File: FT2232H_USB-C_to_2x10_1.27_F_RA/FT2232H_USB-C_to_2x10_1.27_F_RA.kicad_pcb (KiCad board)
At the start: 4 copper layers, 39.8 x 60 mm, 42 parts, among them J1 USB_B_Micro, J2 Conn_02x10_Odd_Even, J3 Conn_02x10_Odd_Even, U1 FT2232HL, U2 93C46BT-I_OT, U3 USBLC6-2SC6, U4 MIC5504-3.3YM5, X1 DSC60xx

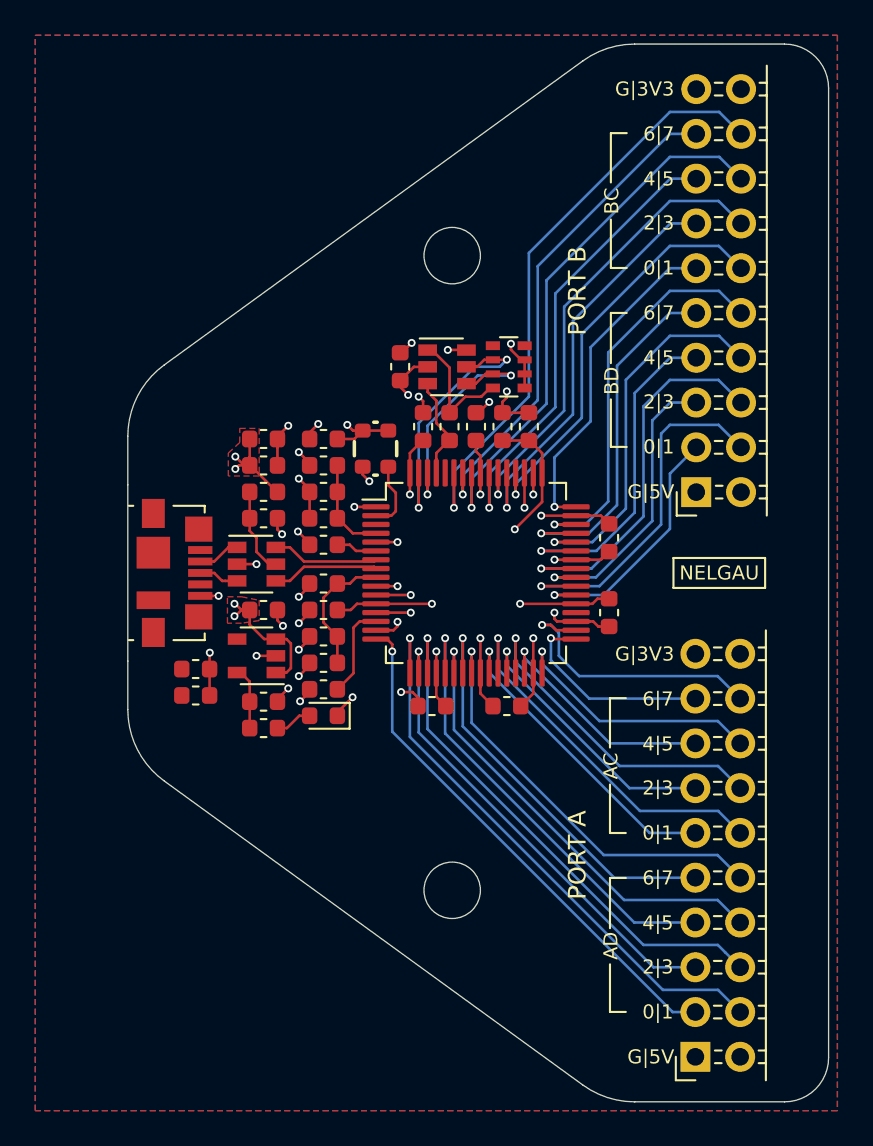
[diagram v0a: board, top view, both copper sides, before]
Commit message: Use USB-C connector instead of micro-USB
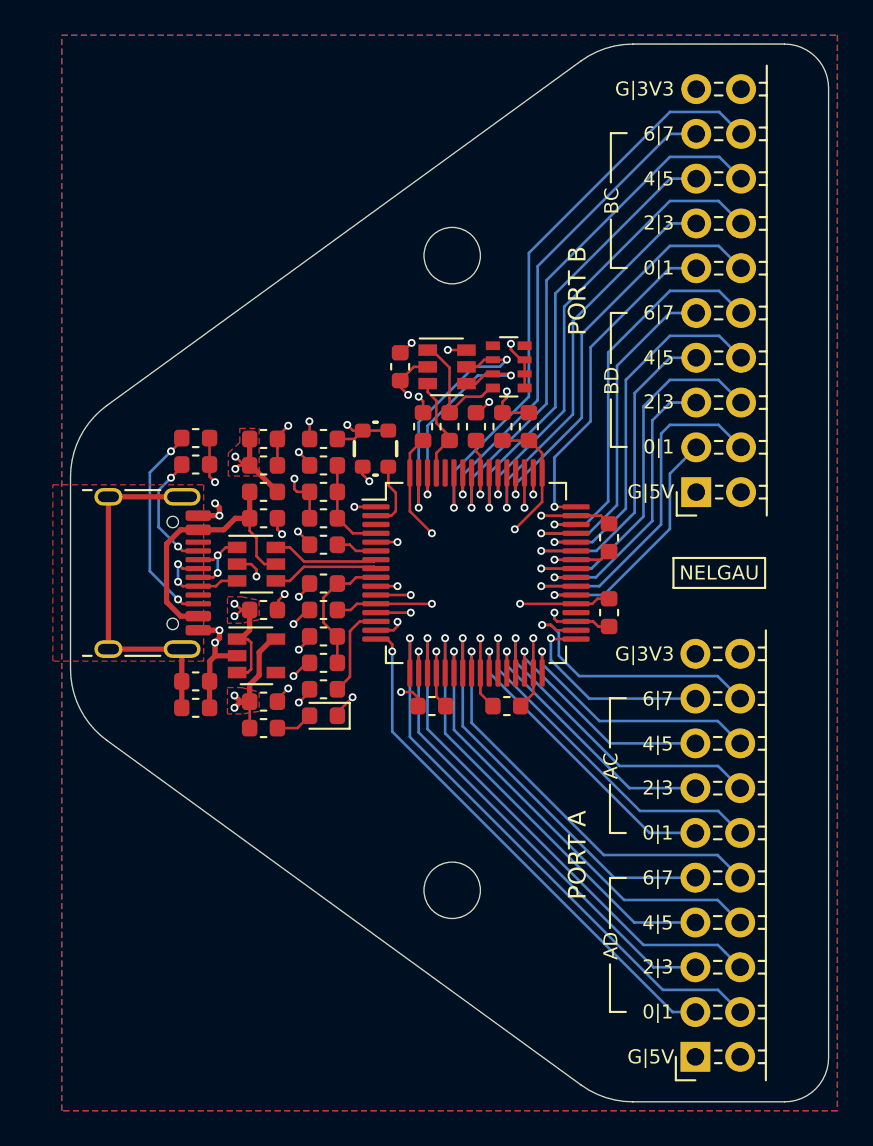
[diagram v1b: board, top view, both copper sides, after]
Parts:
- added R7: 5k1, Resistor_SMD:R_0603_1608Metric, F.Cu at (145.1, 89.4)
- added R8: 5k1, Resistor_SMD:R_0603_1608Metric, F.Cu at (145.1, 90.9)
- J1: value USB_B_Micro -> USB_C_USB2.0; footprint Connector_USB:USB_Micro-B_Molex_47346-0001 -> ng_conn:USB_C_Receptacle_HRO_TYPE-C-31-M-12
- moved J1 2.70 mm to (141.2, 97.0)
- moved R1 2.20 mm to (145.1, 104.7), turned to 0 degrees
- moved C6 0.80 mm to (145.1, 103.2)
- turned U4 to 0 degrees
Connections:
- R1 pad 1: GND -> /USB_SHD
- R1 pad 2: /USB_SHD -> GND
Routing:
- net /USB_SHD: track 0.00 -> 20.5 mm
- net /USB_CC2: track 0.00 -> 11.8 mm, vias 0 -> 2
- net /USB_VBUS: track 4.95 -> 15.8 mm
- net GND: track 53.8 -> 62.2 mm, vias 31 -> 33
- net /USB_CC1: track 0.00 -> 6.90 mm, vias 0 -> 2
- net P3V3: track 30.8 -> 34.9 mm, vias 12 -> 14
- net /xUSB_D+: track 2.28 -> 5.83 mm, vias 0 -> 2
- net P1V8: track 21.6 -> 24.3 mm
- net /xUSB_D-: track 2.42 -> 4.70 mm, vias 0 -> 2
- added copper zone on F.Cu, net /USB_SHD
- added copper zone on F.Cu, net P3V3
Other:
- board size 39.8 x 60 mm -> 43 x 60 mm

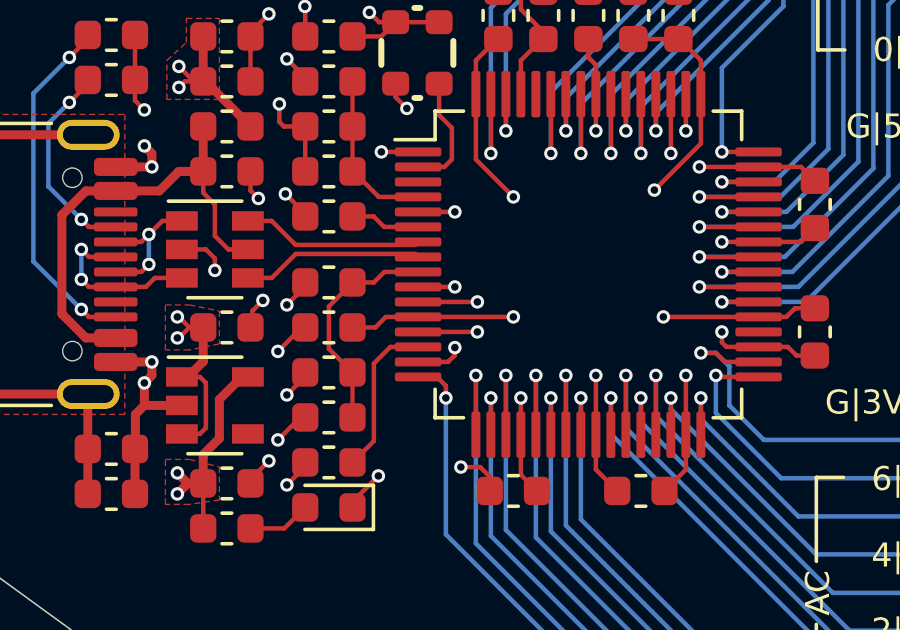
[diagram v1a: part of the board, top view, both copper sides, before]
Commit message: Reduce via usage on FT2232 ground connections
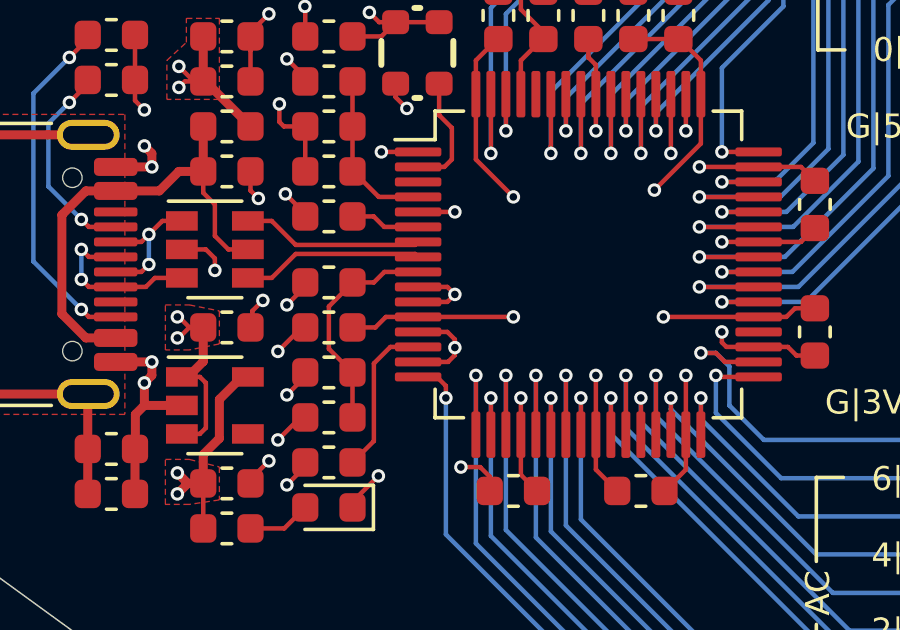
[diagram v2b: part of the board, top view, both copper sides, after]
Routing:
- net GND: track 62.2 -> 61.3 mm, vias 33 -> 31
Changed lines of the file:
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@@
     (thickness 1.2)
     (drawings 63)
-    (tracks 612)
+    (tracks 614)
     (zones 0)
     (modules 44)
@@
   (layers
     (0 F.Cu signal)
-    (1 "In1(GND).Cu" power)
-    (2 "In2(PWR).Cu" power)
+    (1 "In1(GND).Cu" power hide)
+    (2 "In2(PWR).Cu" power hide)
     (31 B.Cu signal)
     (32 B.Adhes user hide)
@@
   )
   (setup
-    (last_trace_width 0.3)
+    (last_trace_width 0.15)
     (user_trace_width 0.3)
     (user_trace_width 0.6)
@@
   (via (at 161.25 100.728) (size 0.45) (drill 0.25) (layers F.Cu B.Cu) (net 1))
   (segment (start 161.25 102.703) (end 161.25 100.728) (width 0.15) (layer F.Cu) (net 1))
-  (via (at 157.3 98.278) (size 0.45) (drill 0.25) (layers F.Cu B.Cu) (net 1))
-  (segment (start 155.325 98.278) (end 157.3 98.278) (width 0.15) (layer F.Cu) (net 1))
-  (via (at 156.54999 97.778) (size 0.45) (drill 0.25) (layers F.Cu B.Cu) (net 1))
-  (segment (start 155.325 97.778) (end 156.54999 97.778) (width 0.15) (layer F.Cu) (net 1))
   (segment (start 167.45 93.778) (end 166.675 93.778) (width 0.15) (layer F.Cu) (net 1))
   (segment (start 168.0875 93.778) (end 167.45 93.778) (width 0.15) (layer F.Cu) (net 1))
@@
   (segment (start 162.75 87.078) (end 162.75 86.728) (width 0.15) (layer F.Cu) (net 1))
   (segment (start 162.5 87.328) (end 162.75 87.078) (width 0.15) (layer F.Cu) (net 1))
-  (segment (start 155.325 99.278) (end 157.3 99.278) (width 0.15) (layer F.Cu) (net 1))
-  (via (at 157.3 99.278) (size 0.45) (drill 0.25) (layers F.Cu B.Cu) (net 1))
   (via (at 156.55 99.799992) (size 0.45) (drill 0.25) (layers F.Cu B.Cu) (net 1))
-  (segment (start 156.55 100.05) (end 156.55 99.799992) (width 0.15) (layer F.Cu) (net 1))
-  (segment (start 156.322 100.278) (end 156.55 100.05) (width 0.15) (layer F.Cu) (net 1))
-  (segment (start 155.325 100.278) (end 156.322 100.278) (width 0.15) (layer F.Cu) (net 1))
   (via (at 150.00001 94.828) (size 0.45) (drill 0.25) (layers F.Cu B.Cu) (net 1))
   (segment (start 149.7375 94.56549) (end 150.00001 94.828) (width 0.15) (layer F.Cu) (net 1))
@@
   (segment (start 148.25 96.528) (end 148.549996 96.827996) (width 0.15) (layer F.Cu) (net 1))
   (segment (start 147.45 96.528) (end 148.25 96.528) (width 0.15) (layer F.Cu) (net 1))
+  (segment (start 156.55 100.05) (end 156.55 99.799992) (width 0.15) (layer F.Cu) (net 1))
+  (segment (start 156.322 100.278) (end 156.55 100.05) (width 0.15) (layer F.Cu) (net 1))
+  (segment (start 155.325 100.278) (end 156.322 100.278) (width 0.15) (layer F.Cu) (net 1))
+  (segment (start 156.55 99.528) (end 156.55 99.799992) (width 0.15) (layer F.Cu) (net 1))
+  (segment (start 156.3 99.278) (end 156.55 99.528) (width 0.15) (layer F.Cu) (net 1))
+  (segment (start 155.325 99.278) (end 156.3 99.278) (width 0.15) (layer F.Cu) (net 1))
+  (segment (start 156.3 97.778) (end 156.55 98.028) (width 0.15) (layer F.Cu) (net 1))
+  (segment (start 156.3 98.278) (end 156.55 98.028) (width 0.15) (layer F.Cu) (net 1))
+  (via (at 156.55 98.028) (size 0.45) (drill 0.25) (layers F.Cu B.Cu) (net 1))
+  (segment (start 155.325 97.778) (end 156.3 97.778) (width 0.15) (layer F.Cu) (net 1))
+  (segment (start 155.325 98.278) (end 156.3 98.278) (width 0.15) (layer F.Cu) (net 1))
   (segment (start 162.975 89.5155) (end 164 89.5155) (width 0.15) (layer F.Cu) (net 2))
   (segment (start 162.5 89.5155) (end 162.975 89.5155) (width 0.15) (layer F.Cu) (net 2))
@@
   (segment (start 163.45 118.478) (end 170.9 125.928) (width 0.3) (layer "In2(PWR).Cu") (net 4))
   (segment (start 149.45 98.778) (end 149.45 104.478) (width 0.3) (layer "In2(PWR).Cu") (net 4))
+  (segment (start 147.65 102.678) (end 147.45 102.678) (width 0.15) (layer F.Cu) (net 4))
+  (segment (start 148.1625 100.2655) (end 147.65 100.778) (width 0.3) (layer F.Cu) (net 4))
+  (segment (start 147.65 100.778) (end 147.45 100.778) (width 0.3) (layer F.Cu) (net 4))
+  (segment (start 148.1625 99.128) (end 148.1625 100.2655) (width 0.3) (layer F.Cu) (net 4))
+  (segment (start 148.1625 89.428) (end 148.1625 90.928) (width 0.3) (layer F.Cu) (net 4))
+  (segment (start 148.2375 90.928) (end 149.7375 92.428) (width 0.3) (layer F.Cu) (net 4))
+  (segment (start 148.1625 90.928) (end 148.2375 90.928) (width 0.3) (layer F.Cu) (net 4))
+  (segment (start 149.45 98.778) (end 149.45 95.878) (width 0.3) (layer "In2(PWR).Cu") (net 4))
+  (segment (start 147.35 93.778) (end 147.35 91.128004) (width 0.3) (layer "In2(PWR).Cu") (net 4))
+  (segment (start 149.45 95.878) (end 147.35 93.778) (width 0.3) (layer "In2(PWR).Cu") (net 4))
+  (segment (start 148.05 102.678) (end 147.45 102.678) (width 0.15) (layer F.Cu) (net 4))
+  (segment (start 148.25 100.978) (end 148.25 102.478) (width 0.15) (layer F.Cu) (net 4))
+  (segment (start 148.25 102.478) (end 148.05 102.678) (width 0.15) (layer F.Cu) (net 4))
+  (segment (start 148.05 100.778) (end 148.25 100.978) (width 0.15) (layer F.Cu) (net 4))
+  (segment (start 147.45 100.778) (end 148.05 100.778) (width 0.15) (layer F.Cu) (net 4))
   (segment (start 142.98 92.708) (end 140.15 92.708) (width 0.3) (layer F.Cu) (net 5))
   (segment (start 144.33 92.708) (end 142.98 92.708) (width 0.3) (layer F.Cu) (net 5))
@@
   (segment (start 164.25 91.353) (end 164.25 92.578) (width 0.15) (layer F.Cu) (net 6))
   (segment (start 160.458147 84.387009) (end 160.259009 84.387009) (width 0.15) (layer F.Cu) (net 6))
-  (segment (start 147.65 102.678) (end 147.45 102.678) (width 0.15) (layer F.Cu) (net 4))
-  (segment (start 148.1625 100.2655) (end 147.65 100.778) (width 0.3) (layer F.Cu) (net 4))
-  (segment (start 147.65 100.778) (end 147.45 100.778) (width 0.3) (layer F.Cu) (net 4))
-  (segment (start 148.1625 99.128) (end 148.1625 100.2655) (width 0.3) (layer F.Cu) (net 4))
-  (segment (start 148.1625 89.428) (end 148.1625 90.928) (width 0.3) (layer F.Cu) (net 4))
-  (segment (start 148.2375 90.928) (end 149.7375 92.428) (width 0.3) (layer F.Cu) (net 4))
-  (segment (start 148.1625 90.928) (end 148.2375 90.928) (width 0.3) (layer F.Cu) (net 4))
-  (segment (start 149.45 98.778) (end 149.45 95.878) (width 0.3) (layer "In2(PWR).Cu") (net 4))
-  (segment (start 147.35 93.778) (end 147.35 91.128004) (width 0.3) (layer "In2(PWR).Cu") (net 4))
-  (segment (start 149.45 95.878) (end 147.35 93.778) (width 0.3) (layer "In2(PWR).Cu") (net 4))
-  (segment (start 148.05 102.678) (end 147.45 102.678) (width 0.15) (layer F.Cu) (net 4))
-  (segment (start 148.25 100.978) (end 148.25 102.478) (width 0.15) (layer F.Cu) (net 4))
-  (segment (start 148.25 102.478) (end 148.05 102.678) (width 0.15) (layer F.Cu) (net 4))
-  (segment (start 148.05 100.778) (end 148.25 100.978) (width 0.15) (layer F.Cu) (net 4))
-  (segment (start 147.45 100.778) (end 148.05 100.778) (width 0.15) (layer F.Cu) (net 4))
   (segment (start 156.025 88.953) (end 154.575 88.953) (width 0.15) (layer F.Cu) (net 6))
   (segment (start 154.1 89.428) (end 153.1375 89.428) (width 0.15) (layer F.Cu) (net 6))

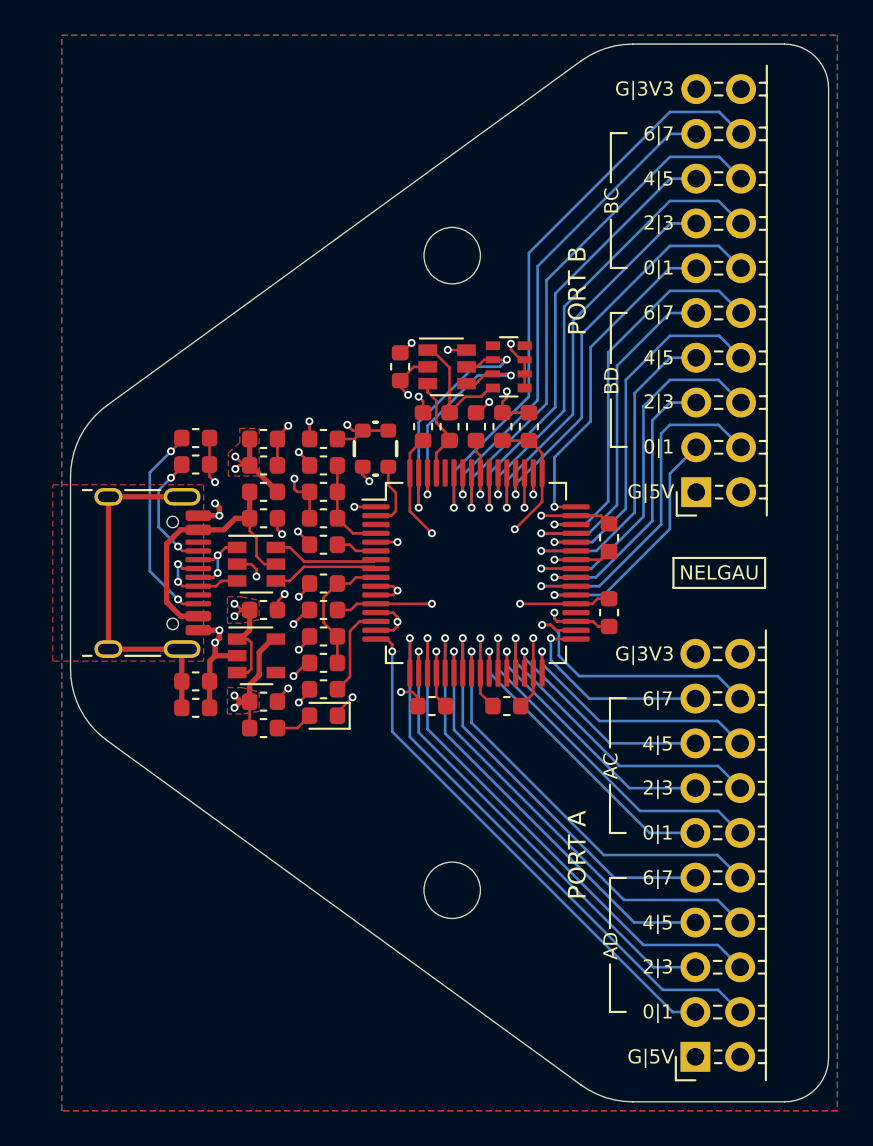
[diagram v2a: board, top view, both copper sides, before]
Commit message: Fix collision between power trace and mouting hole pad
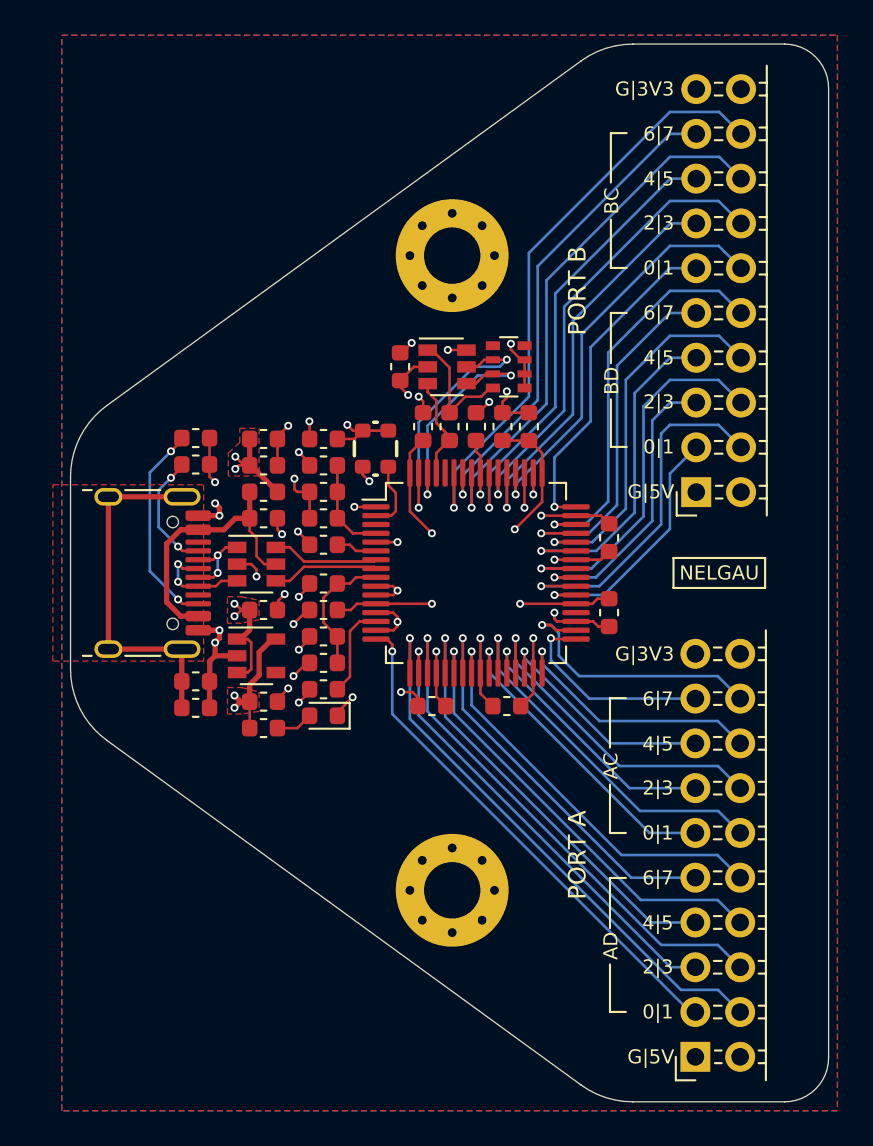
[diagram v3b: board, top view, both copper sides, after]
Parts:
- H1, H2: footprint MountingHole:MountingHole_3.2mm_M3 -> MountingHole:MountingHole_3.2mm_M3_Pad_Via
- R2: value 10k -> 1k
- R6: value 249R -> 1k
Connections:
- net /USB_OSC renamed /USB_CLK
- H1 pad 1: (no net) -> GND
- H2 pad 1: (no net) -> GND
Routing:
- net USB_5V: track 102.3 -> 102.9 mm
- net /AD1: track 32.8 -> 32.2 mm
- net /AD3: track 30.5 -> 29.9 mm
- net /AD0: track 29.8 -> 29.2 mm
- net /AD7: track 24.1 -> 23.6 mm
- net /AD2: track 27.0 -> 26.5 mm
- net /AD6: track 23.7 -> 23.2 mm
- net /AD5: track 26.4 -> 25.9 mm
- net /AD4: track 26.0 -> 25.5 mm
